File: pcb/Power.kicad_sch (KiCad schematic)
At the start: 12 parts, among them U4 LD39050PU33R, U5 TLV61048, U6 LDK320AM120R

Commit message: Updated PCB
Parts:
- added C28: 1u, Capacitor_SMD:C_0603_1608Metric, symbol Device:C
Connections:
- net 13.12V: now also C28.1
- net GND: now also C28.2
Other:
- moved on the sheet: C27, U6
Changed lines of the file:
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@@
   (junction (at 106.68 76.2) (diameter 0) (color 0 0 0 0)
   )
+  (junction (at 172.72 116.84) (diameter 0) (color 0 0 0 0)
+  )
   (junction (at 106.68 73.66) (diameter 0) (color 0 0 0 0)
   )
-  (junction (at 182.88 128.27) (diameter 0) (color 0 0 0 0)
-  )
-  (junction (at 173.99 116.84) (diameter 0) (color 0 0 0 0)
+  (junction (at 185.42 128.27) (diameter 0) (color 0 0 0 0)
+  )
+  (junction (at 176.53 116.84) (diameter 0) (color 0 0 0 0)
   )
   (junction (at 123.19 88.9) (diameter 0) (color 0 0 0 0)
@@
   (junction (at 113.03 121.92) (diameter 0) (color 0 0 0 0)
   )
-  (junction (at 191.77 116.84) (diameter 0) (color 0 0 0 0)
+  (junction (at 194.31 116.84) (diameter 0) (color 0 0 0 0)
   )
   (junction (at 143.51 127) (diameter 0) (color 0 0 0 0)
@@
   )
   (no_connect (at 133.35 78.74))
-  (wire (pts (xy 191.77 116.84) (xy 190.5 116.84))
-    (stroke (width 0) (type default))
-  )
-  (wire (pts (xy 191.77 125.73) (xy 191.77 128.27))
+  (wire (pts (xy 194.31 116.84) (xy 193.04 116.84))
+    (stroke (width 0) (type default))
+  )
+  (wire (pts (xy 172.72 116.84) (xy 176.53 116.84))
+    (stroke (width 0) (type default))
+  )
+  (wire (pts (xy 194.31 125.73) (xy 194.31 128.27))
     (stroke (width 0) (type default))
   )
@@
     (stroke (width 0) (type default))
   )
-  (wire (pts (xy 191.77 116.84) (xy 193.04 116.84))
+  (wire (pts (xy 194.31 116.84) (xy 195.58 116.84))
     (stroke (width 0) (type default))
   )
@@
     (stroke (width 0) (type default))
   )
-  (wire (pts (xy 175.26 119.38) (xy 173.99 119.38))
-    (stroke (width 0) (type default))
-  )
-  (wire (pts (xy 191.77 118.11) (xy 191.77 116.84))
+  (wire (pts (xy 177.8 119.38) (xy 176.53 119.38))
+    (stroke (width 0) (type default))
+  )
+  (wire (pts (xy 194.31 118.11) (xy 194.31 116.84))
     (stroke (width 0) (type default))
   )
@@
     (stroke (width 0) (type default))
   )
-  (wire (pts (xy 182.88 129.54) (xy 182.88 128.27))
+  (wire (pts (xy 185.42 129.54) (xy 185.42 128.27))
     (stroke (width 0) (type default))
   )
@@
     (stroke (width 0) (type default))
   )
+  (wire (pts (xy 172.72 125.73) (xy 172.72 128.27))
+    (stroke (width 0) (type default))
+  )
   (wire (pts (xy 114.3 124.46) (xy 110.49 124.46))
     (stroke (width 0) (type default))
@@
     (stroke (width 0) (type default))
   )
-  (wire (pts (xy 154.94 116.84) (xy 173.99 116.84))
+  (wire (pts (xy 154.94 116.84) (xy 172.72 116.84))
+    (stroke (width 0) (type default))
+  )
+  (wire (pts (xy 172.72 128.27) (xy 185.42 128.27))
     (stroke (width 0) (type default))
   )
@@
     (stroke (width 0) (type default))
   )
-  (wire (pts (xy 182.88 128.27) (xy 182.88 127))
+  (wire (pts (xy 185.42 128.27) (xy 185.42 127))
     (stroke (width 0) (type default))
   )
@@
     (stroke (width 0) (type default))
   )
-  (wire (pts (xy 173.99 119.38) (xy 173.99 116.84))
-    (stroke (width 0) (type default))
-  )
-  (wire (pts (xy 182.88 128.27) (xy 191.77 128.27))
-    (stroke (width 0) (type default))
-  )
-  (wire (pts (xy 173.99 116.84) (xy 175.26 116.84))
+  (wire (pts (xy 176.53 119.38) (xy 176.53 116.84))
+    (stroke (width 0) (type default))
+  )
+  (wire (pts (xy 185.42 128.27) (xy 194.31 128.27))
+    (stroke (width 0) (type default))
+  )
+  (wire (pts (xy 176.53 116.84) (xy 177.8 116.84))
     (stroke (width 0) (type default))
   )
@@
   )
   (wire (pts (xy 113.03 121.92) (xy 113.03 116.84))
+    (stroke (width 0) (type default))
+  )
+  (wire (pts (xy 172.72 116.84) (xy 172.72 118.11))
     (stroke (width 0) (type default))
   )
@@
     (effects (font (size 1.27 1.27)) (justify left top))
   )
-  (label "13.12V" (at 161.29 116.84 0) (fields_autoplaced)
+  (label "13.12V" (at 163.83 116.84 0) (fields_autoplaced)
     (effects (font (size 1.27 1.27)) (justify left bottom))
   )
-  (hierarchical_label "12V" (shape output) (at 193.04 116.84 0) (fields_autoplaced)
+  (hierarchical_label "12V" (shape output) (at 195.58 116.84 0) (fields_autoplaced)
     (effects (font (size 1.27 1.27)) (justify left))
   )
@@
     )
   )
-  (symbol (lib_id "Signal Generator Components:LDK320AM120R") (at 182.88 119.38 0) (unit 1)
-    (in_bom yes) (on_board yes) (dnp no) (fields_autoplaced)
-    (property "Reference" "U6" (at 182.88 110.49 0)
-      (effects (font (size 1.27 1.27)))
-    )
-    (property "Value" "LDK320AM120R" (at 182.88 113.03 0)
-      (effects (font (size 1.27 1.27)))
-    )
-    (property "Footprint" "Signal Generator Components:LDK320AM120R" (at 177.8 110.49 0)
-      (effects (font (size 1.27 1.27)) hide)
-    )
-    (property "Datasheet" "" (at 182.88 119.38 0)
-      (effects (font (size 1.27 1.27)) hide)
-    )
-    (property "PN" "LDK320AM120R" (at 182.88 119.38 0)
+  (symbol (lib_id "Signal Generator Components:LDK320AM120R") (at 185.42 119.38 0) (unit 1)
+    (in_bom yes) (on_board yes) (dnp no) (fields_autoplaced)
+    (property "Reference" "U6" (at 185.42 110.49 0)
+      (effects (font (size 1.27 1.27)))
+    )
+    (property "Value" "LDK320AM120R" (at 185.42 113.03 0)
+      (effects (font (size 1.27 1.27)))
+    )
+    (property "Footprint" "Signal Generator Components:LDK320AM120R" (at 180.34 110.49 0)
+      (effects (font (size 1.27 1.27)) hide)
+    )
+    (property "Datasheet" "" (at 185.42 119.38 0)
+      (effects (font (size 1.27 1.27)) hide)
+    )
+    (property "PN" "LDK320AM120R" (at 185.42 119.38 0)
       (effects (font (size 1.27 1.27)) hide)
     )
@@
     )
   )
-  (symbol (lib_id "Device:C") (at 191.77 121.92 0) (unit 1)
-    (in_bom yes) (on_board yes) (dnp no) (fields_autoplaced)
-    (property "Reference" "C27" (at 195.58 121.285 0)
-      (effects (font (size 1.27 1.27)) (justify left))
-    )
-    (property "Value" "1u" (at 195.58 123.825 0)
-      (effects (font (size 1.27 1.27)) (justify left))
-    )
-    (property "Footprint" "Capacitor_SMD:C_0603_1608Metric" (at 192.7352 125.73 0)
-      (effects (font (size 1.27 1.27)) hide)
-    )
-    (property "Datasheet" "~" (at 191.77 121.92 0)
-      (effects (font (size 1.27 1.27)) hide)
-    )
-    (property "PN" "GCM188R71C105KA64D" (at 191.77 121.92 0)
+  (symbol (lib_id "Device:C") (at 194.31 121.92 0) (unit 1)
+    (in_bom yes) (on_board yes) (dnp no) (fields_autoplaced)
+    (property "Reference" "C27" (at 198.12 121.285 0)
+      (effects (font (size 1.27 1.27)) (justify left))
+    )
+    (property "Value" "1u" (at 198.12 123.825 0)
+      (effects (font (size 1.27 1.27)) (justify left))
+    )
+    (property "Footprint" "Capacitor_SMD:C_0603_1608Metric" (at 195.2752 125.73 0)
+      (effects (font (size 1.27 1.27)) hide)
+    )
+    (property "Datasheet" "~" (at 194.31 121.92 0)
+      (effects (font (size 1.27 1.27)) hide)
+    )
+    (property "PN" "GCM188R71C105KA64D" (at 194.31 121.92 0)
       (effects (font (size 1.27 1.27)) hide)
     )
@@
         (path "/f6255c48-6253-4c69-a6db-1ceaf4eff04d/755a5482-c972-48ba-877b-a349f74d45fc"
           (reference "#PWR0133") (unit 1)
+        )
+      )
+    )
+  )
+  (symbol (lib_id "Device:C") (at 172.72 121.92 0) (mirror y) (unit 1)
+    (in_bom yes) (on_board yes) (dnp no)
+    (property "Reference" "C28" (at 168.91 121.285 0)
+      (effects (font (size 1.27 1.27)) (justify left))
+    )
+    (property "Value" "1u" (at 168.91 123.825 0)
+      (effects (font (size 1.27 1.27)) (justify left))
+    )
+    (property "Footprint" "Capacitor_SMD:C_0603_1608Metric" (at 171.7548 125.73 0)
+      (effects (font (size 1.27 1.27)) hide)
+    )
+    (property "Datasheet" "~" (at 172.72 121.92 0)
+      (effects (font (size 1.27 1.27)) hide)
+    )
+    (property "PN" "GCM188R71C105KA64D" (at 172.72 121.92 0)
+      (effects (font (size 1.27 1.27)) hide)
+    )
+    (pin "1")
+    (pin "2")
+    (instances
+      (project "Signal Generator"
+        (path "/f6255c48-6253-4c69-a6db-1ceaf4eff04d/755a5482-c972-48ba-877b-a349f74d45fc"
+          (reference "C28") (unit 1)
         )
       )
@@
     )
   )
-  (symbol (lib_id "power:GND") (at 182.88 129.54 0) (unit 1)
-    (in_bom yes) (on_board yes) (dnp no) (fields_autoplaced)
-    (property "Reference" "#PWR010" (at 182.88 135.89 0)
-      (effects (font (size 1.27 1.27)) hide)
-    )
-    (property "Value" "GND" (at 182.88 134.62 0)
-      (effects (font (size 1.27 1.27)))
-    )
-    (property "Footprint" "" (at 182.88 129.54 0)
-      (effects (font (size 1.27 1.27)) hide)
-    )
-    (property "Datasheet" "" (at 182.88 129.54 0)
-      (effects (font (size 1.27 1.27)) hide)
-    )
+  (symbol (lib_id "power:GND") (at 185.42 129.54 0) (unit 1)
+    (in_bom yes) (on_board yes) (dnp no) (fields_autoplaced)
+    (property "Reference" "#PWR010" (at 185.42 135.89 0)
+      (effects (font (size 1.27 1.27)) hide)
+    )
+    (property "Value" "GND" (at 185.42 134.62 0)
+      (effects (font (size 1.27 1.27)))
+    )
+    (property "Footprint" "" (at 185.42 129.54 0)
+      (effects (font (size 1.27 1.27)) hide)
+    )
+    (property "Datasheet" "" (at 185.42 129.54 0)
+      (effects (font (size 1.27 1.27)) hide)
+    )

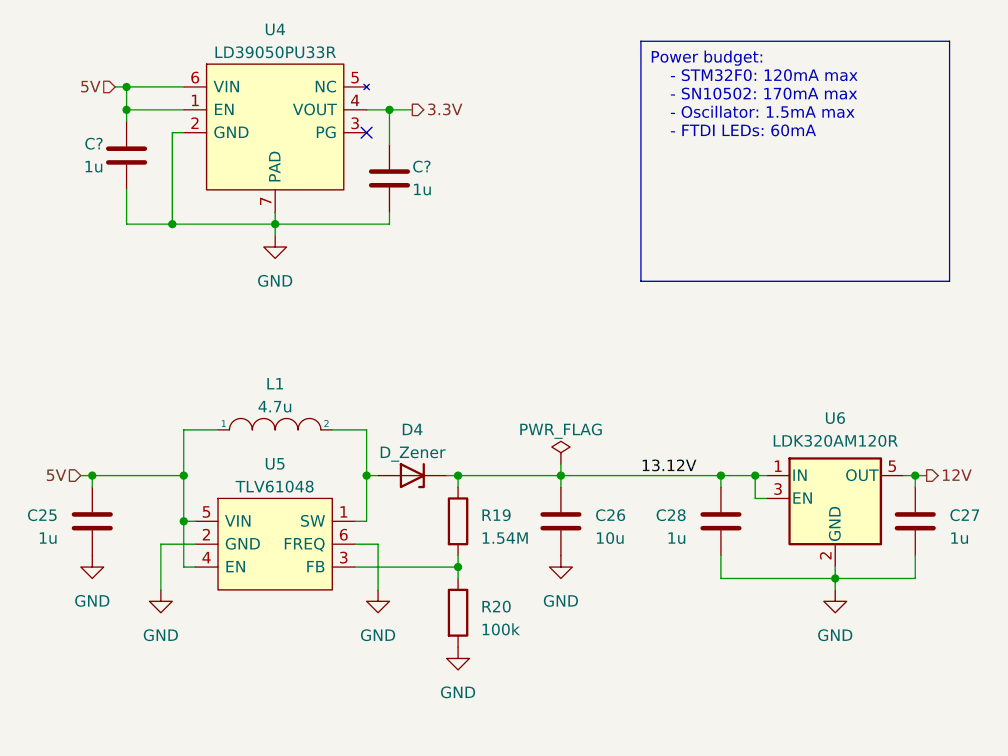
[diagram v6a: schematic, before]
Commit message: Fixed FTDI connection to the stm32
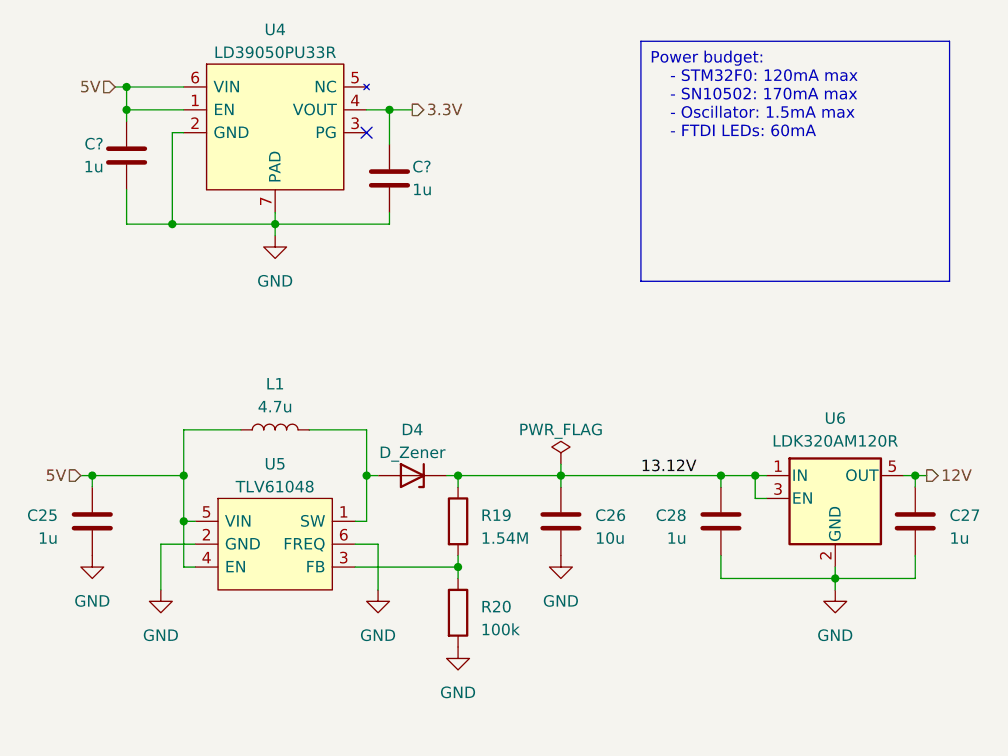
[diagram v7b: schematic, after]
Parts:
- removed L1: 4.7u, Signal Generator Components:XAL4030, symbol pspice:INDUCTOR
- added L1: 4.7u, Signal Generator Components:XAL4030, symbol Device:L
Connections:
- net 5V: now also L1.1
- net at D4.2 (A), U5.1 (SW): now also L1.2
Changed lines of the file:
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@@
-    (stroke (width 0) (type default))
-  )
-  (wire (pts (xy 129.54 111.76) (xy 133.35 111.76))
     (stroke (width 0) (type default))
   )
@@
     (stroke (width 0) (type default))
   )
-  (wire (pts (xy 113.03 111.76) (xy 116.84 111.76))
+  (wire (pts (xy 113.03 111.76) (xy 119.38 111.76))
     (stroke (width 0) (type default))
   )
@@
   )
   (wire (pts (xy 185.42 128.27) (xy 194.31 128.27))
+    (stroke (width 0) (type default))
+  )
+  (wire (pts (xy 127 111.76) (xy 133.35 111.76))
     (stroke (width 0) (type default))
   )
@@
     )
   )
-  (symbol (lib_id "pspice:INDUCTOR") (at 123.19 111.76 0) (unit 1)
-    (in_bom yes) (on_board yes) (dnp no) (fields_autoplaced)
-    (property "Reference" "L1" (at 123.19 106.68 0)
-      (effects (font (size 1.27 1.27)))
-    )
-    (property "Value" "4.7u" (at 123.19 109.22 0)
-      (effects (font (size 1.27 1.27)))
-    )
-    (property "Footprint" "Signal Generator Components:XAL4030" (at 123.19 111.76 0)
-      (effects (font (size 1.27 1.27)) hide)
-    )
-    (property "Datasheet" "~" (at 123.19 111.76 0)
-      (effects (font (size 1.27 1.27)) hide)
-    )
-    (property "PN" "XAL4030-472MEC" (at 123.19 111.76 0)
-      (effects (font (size 1.27 1.27)) hide)
-    )
-    (pin "1")
-    (pin "2")
-    (instances
-      (project "Signal Generator"
-        (path "/f6255c48-6253-4c69-a6db-1ceaf4eff04d/755a5482-c972-48ba-877b-a349f74d45fc"
-          (reference "L1") (unit 1)
-        )
-      )
-    )
-  )
   (symbol (lib_id "Device:C") (at 106.68 81.28 0) (mirror y) (unit 1)
     (in_bom yes) (on_board yes) (dnp no)
@@
         )
       )
+    )
+  )
+  (symbol (lib_id "Device:L") (at 123.19 111.76 90) (unit 1)
+    (in_bom yes) (on_board yes) (dnp no)
+    (property "Reference" "L1" (at 123.19 106.68 90)
+      (effects (font (size 1.27 1.27)))
+    )
+    (property "Value" "4.7u" (at 123.19 109.22 90)
+      (effects (font (size 1.27 1.27)))
+    )
+    (property "Footprint" "Signal Generator Components:XAL4030" (at 123.19 111.76 0)
+      (effects (font (size 1.27 1.27)) hide)
+    )
+    (property "Datasheet" "~" (at 123.19 111.76 0)
+      (effects (font (size 1.27 1.27)) hide)
+    )
+    (property "PN" "XAL4030-472MEC" (at 123.19 111.76 0)
+      (effects (font (size 1.27 1.27)) hide)
+    )
+    (pin "1")
+    (pin "2")
+    (instances
+      (project "Signal Generator"
+        (path "/f6255c48-6253-4c69-a6db-1ceaf4eff04d/755a5482-c972-48ba-877b-a349f74d45fc"
+          (reference "L1") (unit 1)
+        )
+      )
